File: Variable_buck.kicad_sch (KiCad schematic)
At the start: 18 parts, among them U2 LV14540DDAR

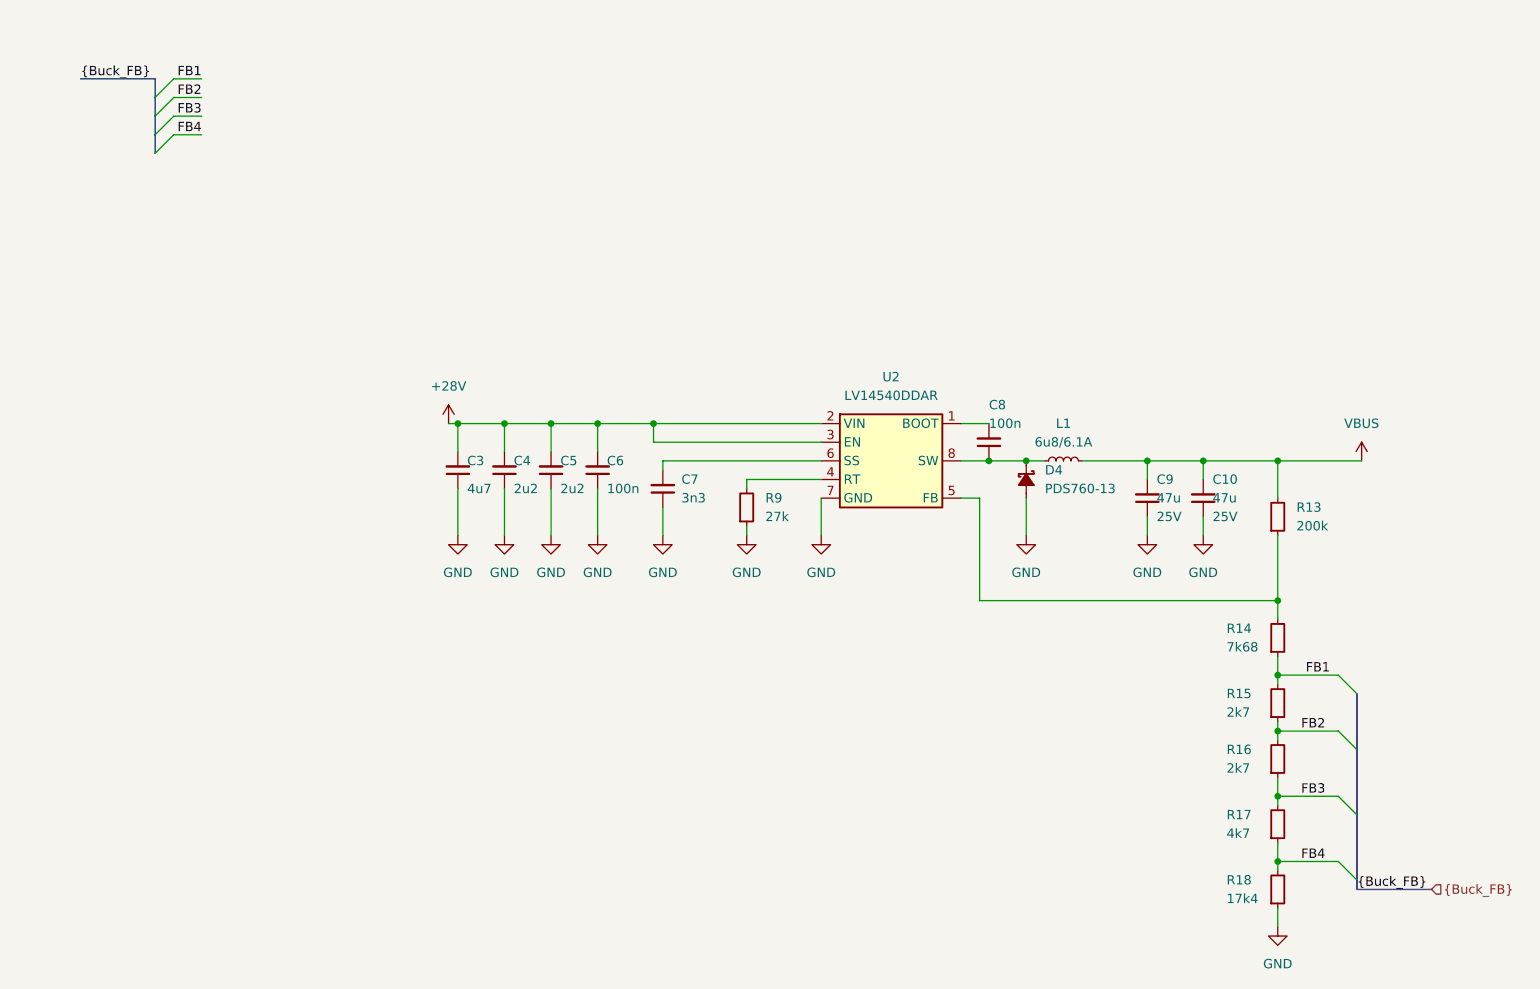
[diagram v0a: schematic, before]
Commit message: [#62623] Improve schematic, change 3V3 buck inductor, correct SPI, add testpoint
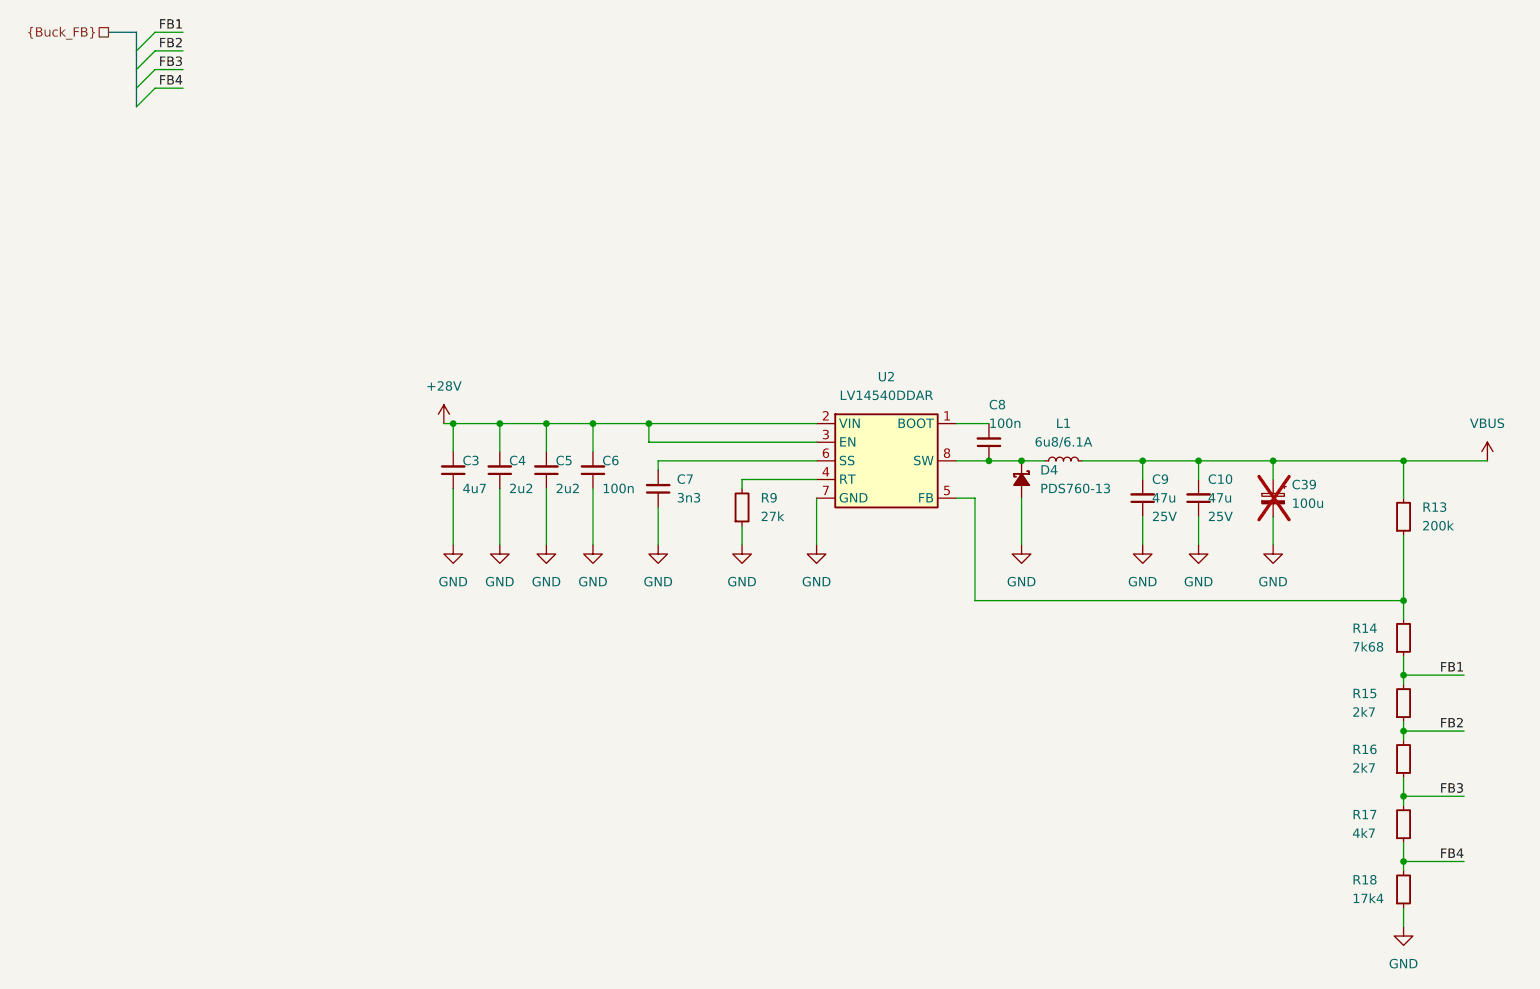
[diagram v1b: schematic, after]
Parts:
- added C39: C_Pol_100u_35V_Panasonic-FP-D8-D6.3mm-H7.7mm, antmicro-footprints:C_Pol_Panasonic-D8-D6.3mm-H7.7mm, symbol antmicroCapacitorspol:C_Pol_100u_35V_Panasonic-FP-D8-D6.3mm-H7.7mm
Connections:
- net GND: now also C39.2
- net VBUS: now also C39.1
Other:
- moved on the sheet: C10, C3, C4, C5, C6, C7, C9, D4, R13, R14, R15, R16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

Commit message: [#62623] Change hierarchy implementation
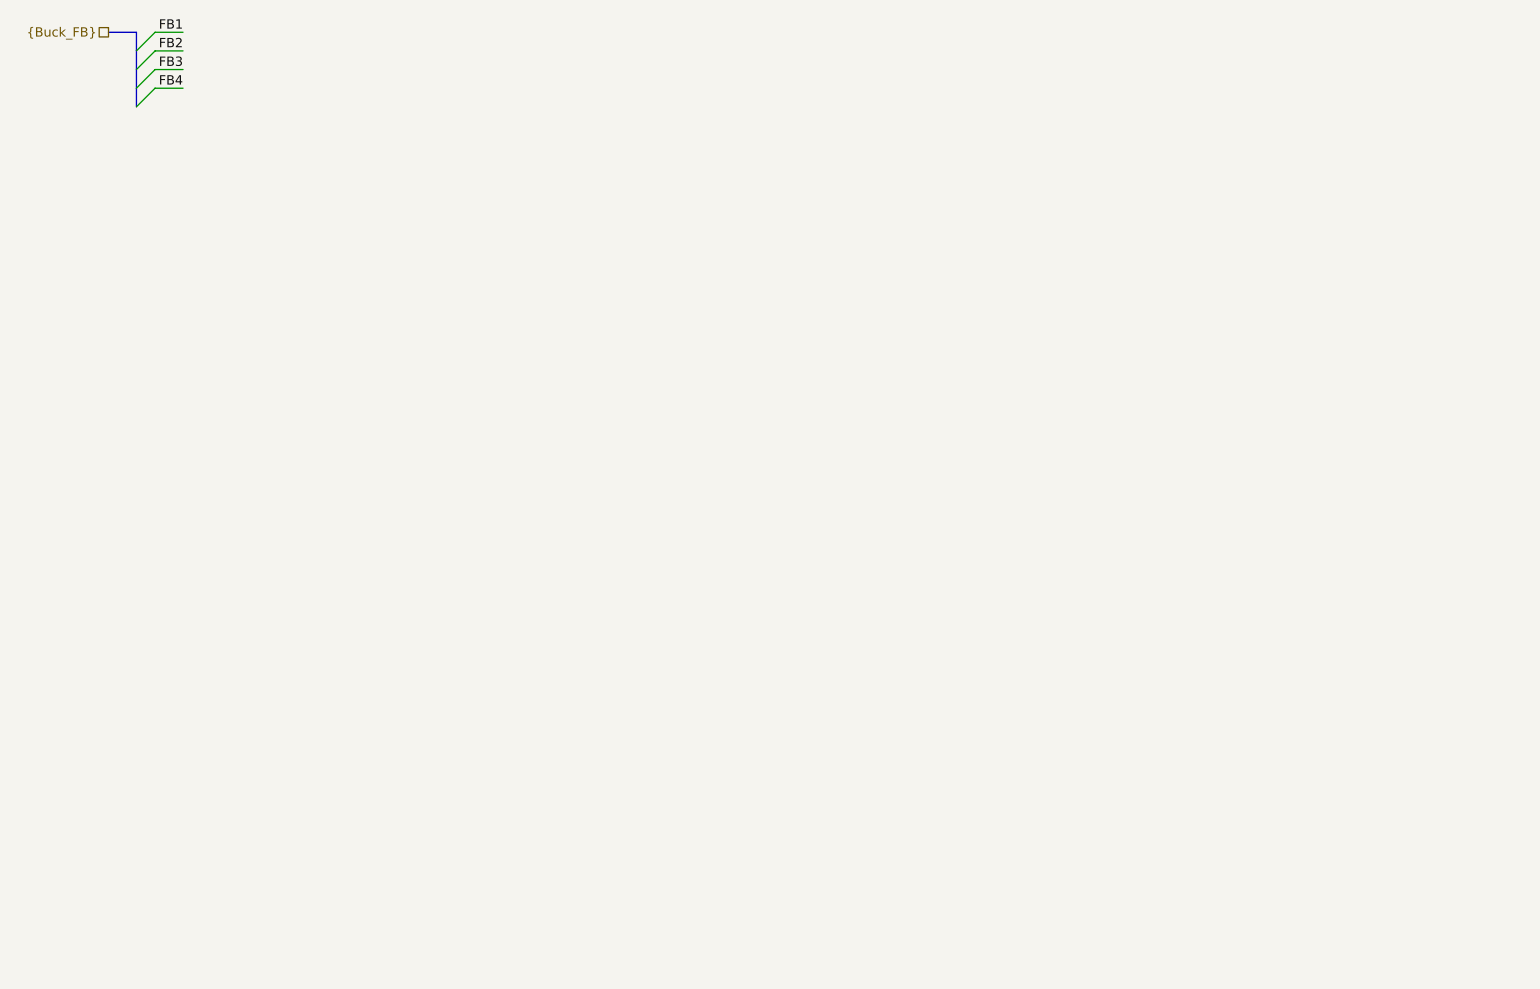
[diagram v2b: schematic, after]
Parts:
- removed C10, C9: C_47u_25V_1206, antmicro-footprints:C_1206_3216Metric, symbol antmicroCapacitorsmisc:C_47u_25V_1206
- removed C3: C_4u7_1210_100V, antmicro-footprints:C_1210_3225Metric, symbol antmicroCapacitorsmisc:C_4u7_1210_100V
- removed C39: C_Pol_100u_35V_Panasonic-FP-D8-D6.3mm-H7.7mm, antmicro-footprints:C_Pol_Panasonic-D8-D6.3mm-H7.7mm, symbol antmicroCapacitorspol:C_Pol_100u_35V_Panasonic-FP-D8-D6.3mm-H7.7mm
- removed C4, C5: C_2u2_1210, antmicro-footprints:C_1210_3225Metric, symbol antmicroCapacitorsmisc:C_2u2_1210
- removed C6, C8: C_100n_100V_X7R_0603, antmicro-footprints:C_0603_1608Metric, symbol antmicroCapacitors0603:C_100n_100V_X7R_0603
- removed C7: C_3n3_0402, antmicro-footprints:C_0402_1005Metric, symbol antmicroCapacitors0402:C_3n3_0402
- removed D4: PDS760, antmicro-footprints:PowerDI5, symbol antmicroDiodesRectifiersSingle:PDS760
- removed L1: L_6u8_6.1A_MPS-MPL-AL5050, antmicro-footprints:L_MPS-MPL-AL5050, symbol antmicroFixedInductors:L_6u8_6.1A_MPS-MPL-AL5050
- removed R13: R_200k_0402, antmicro-footprints:R_0402_1005Metric, symbol antmicroResistors0402:R_200k_0402
- removed R14: R_7k68_0402, antmicro-footprints:R_0402_1005Metric, symbol antmicroResistors0402:R_7k68_0402
- removed R15, R16: R_2k7_0402, antmicro-footprints:R_0402_1005Metric, symbol antmicroResistors0402:R_2k7_0402
- removed R17: R_4k7_0402, antmicro-footprints:R_0402_1005Metric, symbol antmicroResistors0402:R_4k7_0402
- removed R18: R_17k4_0402, antmicro-footprints:R_0402_1005Metric, symbol antmicroResistors0402:R_17k4_0402
- removed R9: R_27k_0402, antmicro-footprints:R_0402_1005Metric, symbol antmicroResistors0402:R_27k_0402
- removed U2: LV14540DDAR, antmicro-footprints:SOIC-8-1EP_3.9x4.9x1.75mm_P1.27mm_EP_vias, symbol antmicroDCDCConverters:LV14540DDAR
